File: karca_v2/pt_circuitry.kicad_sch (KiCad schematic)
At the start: 11 parts, among them U10 TLV9304xD, U9 TLV9304xD

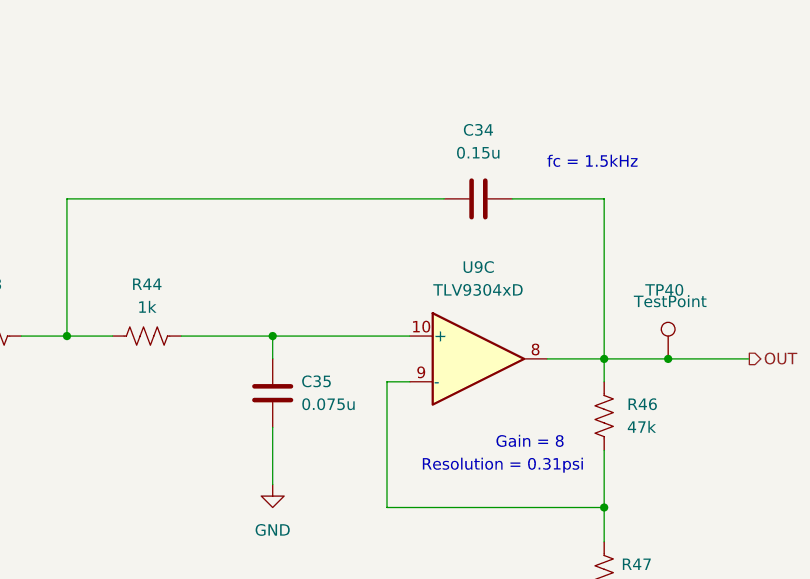
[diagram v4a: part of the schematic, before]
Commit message: changed capacitor values and sizes for production
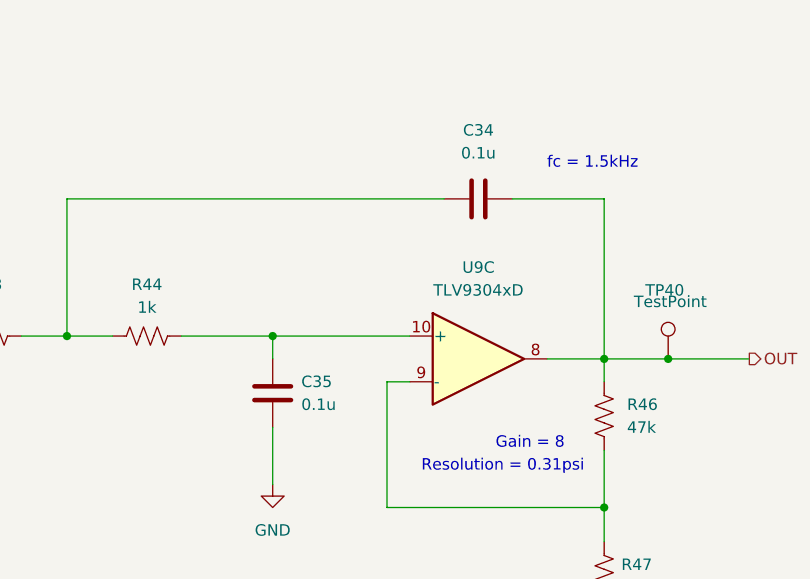
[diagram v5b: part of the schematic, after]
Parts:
- C34: value 0.15u -> 0.1u
- C35: value 0.075u -> 0.1u
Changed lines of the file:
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@@
       (effects (font (size 1.27 1.27)))
     )
-    (property "Value" "0.15u" (at 191.516 53.086 90)
+    (property "Value" "0.1u" (at 191.516 53.086 90)
       (effects (font (size 1.27 1.27)))
     )
@@
       (effects (font (size 1.27 1.27)) (justify left))
     )
-    (property "Value" "0.075u" (at 171.831 81.026 0)
-      (effects (font (size 1.27 1.27)) (justify left))
-    )
+    (property "Value" "0.1u" (at 171.831 81.026 0)
+      (effects (font (size 1.27 1.27)) (justify left))
+    )

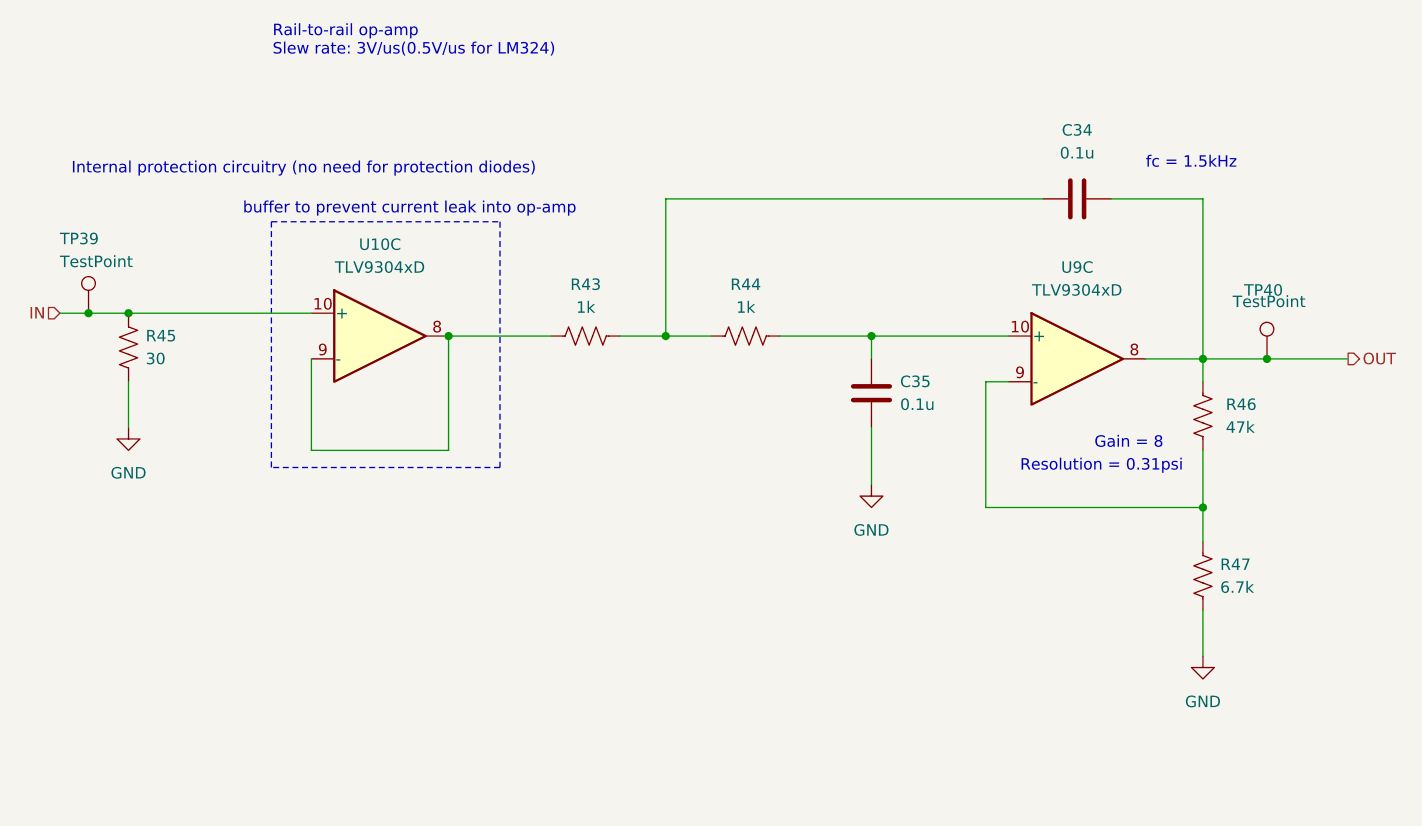
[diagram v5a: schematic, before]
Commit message: cleaned up documentation. Added production files and BOM. Marked Thermocouple components and THT components as DNP (excluded them from BOM too) to match version sent to JLCPCB for fabrication
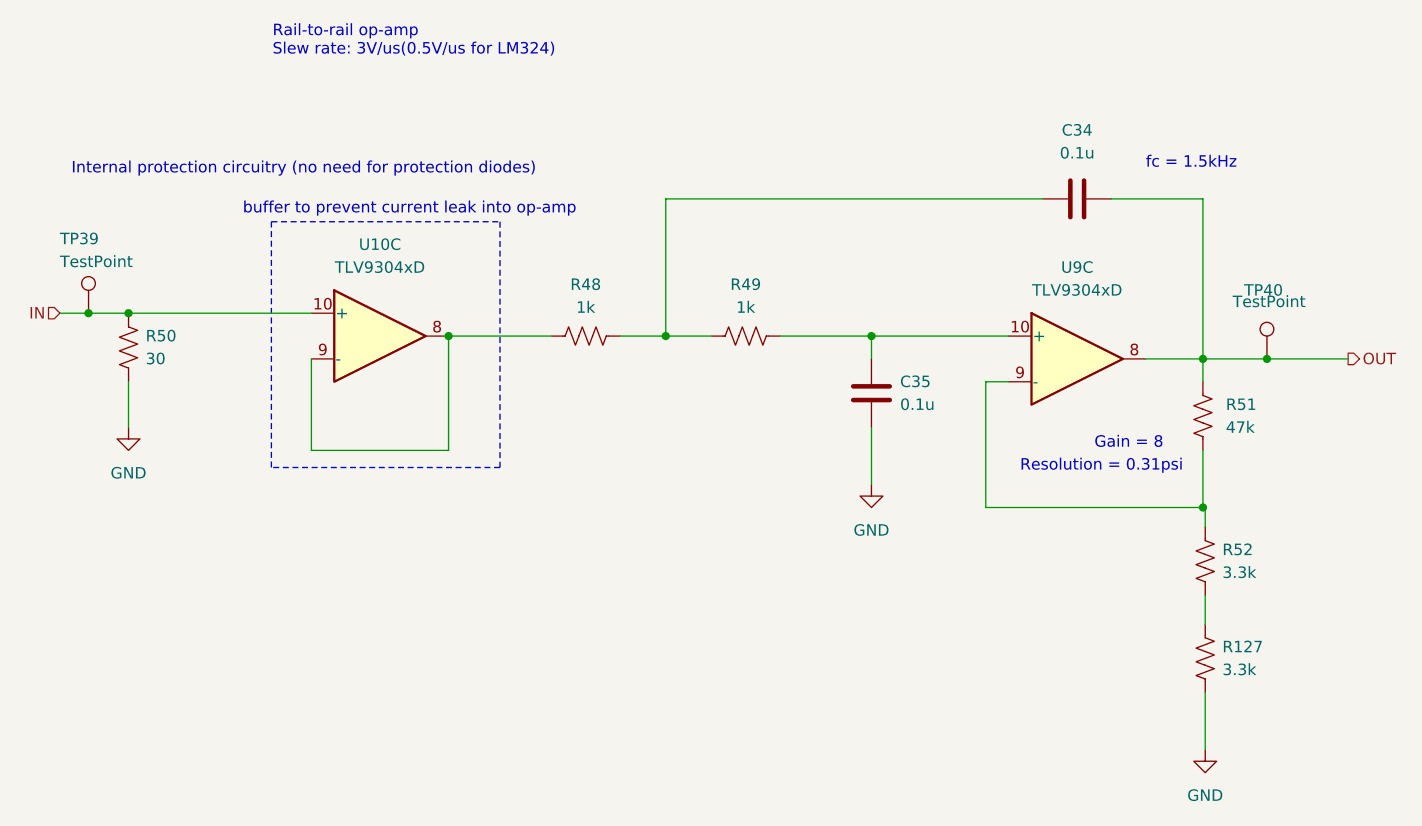
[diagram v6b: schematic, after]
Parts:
- added R127: 3.3k, Resistor_SMD:R_0402_1005Metric, symbol Device:R_US
- R52: renamed from R47; value 6.7k -> 3.3k; footprint Resistor_SMD:R_1206_3216Metric -> Resistor_SMD:R_0402_1005Metric
- renumbered R43 to R48, R44 to R49, R45 to R50, R46 to R51
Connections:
- net GND: now also R127.1; no longer R52.1
- new net: R127.2, R52.1
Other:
- company: (none) -> Rice Eclipse
- title: (none) -> kARCA 2.0 Engine Control System
- moved on the sheet: R52
